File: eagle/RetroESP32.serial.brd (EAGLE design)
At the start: 71.2 x 115 mm, 68 parts, among them J1 AUDIO_JACK_3.5MM_KIT, J2 SPKR, J3 Batt Conn, J5 503182-1852_503182-1852, J6 USB4110-GF-A, Q3 DMG3415U-7, Q4 mmbt2222, Q5 mmbt2222, U1 ESP32-WROVER_ESP32-WROVER, U3 AP2112-3.3, U4 MCP73831T-2ACI/OT, U6 LM4875

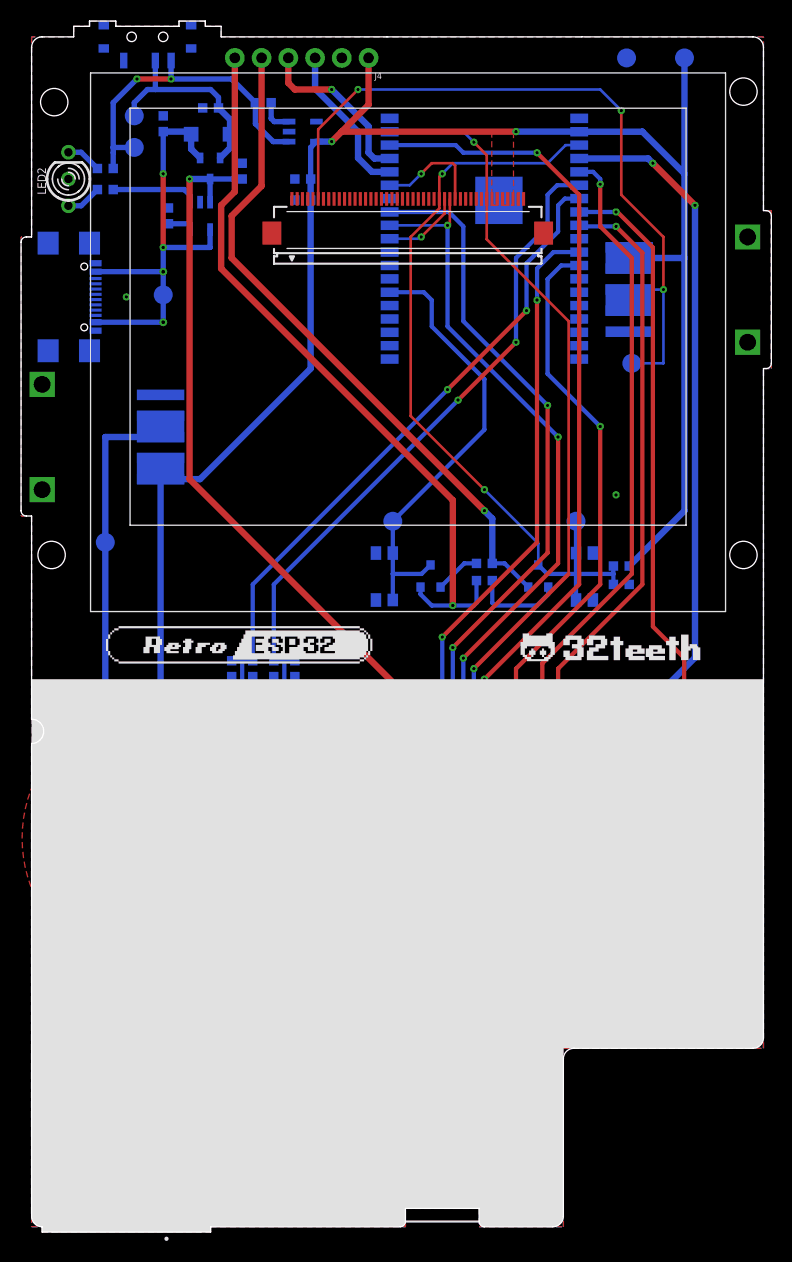
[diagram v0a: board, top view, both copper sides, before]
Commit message: updated CC1/2 pins
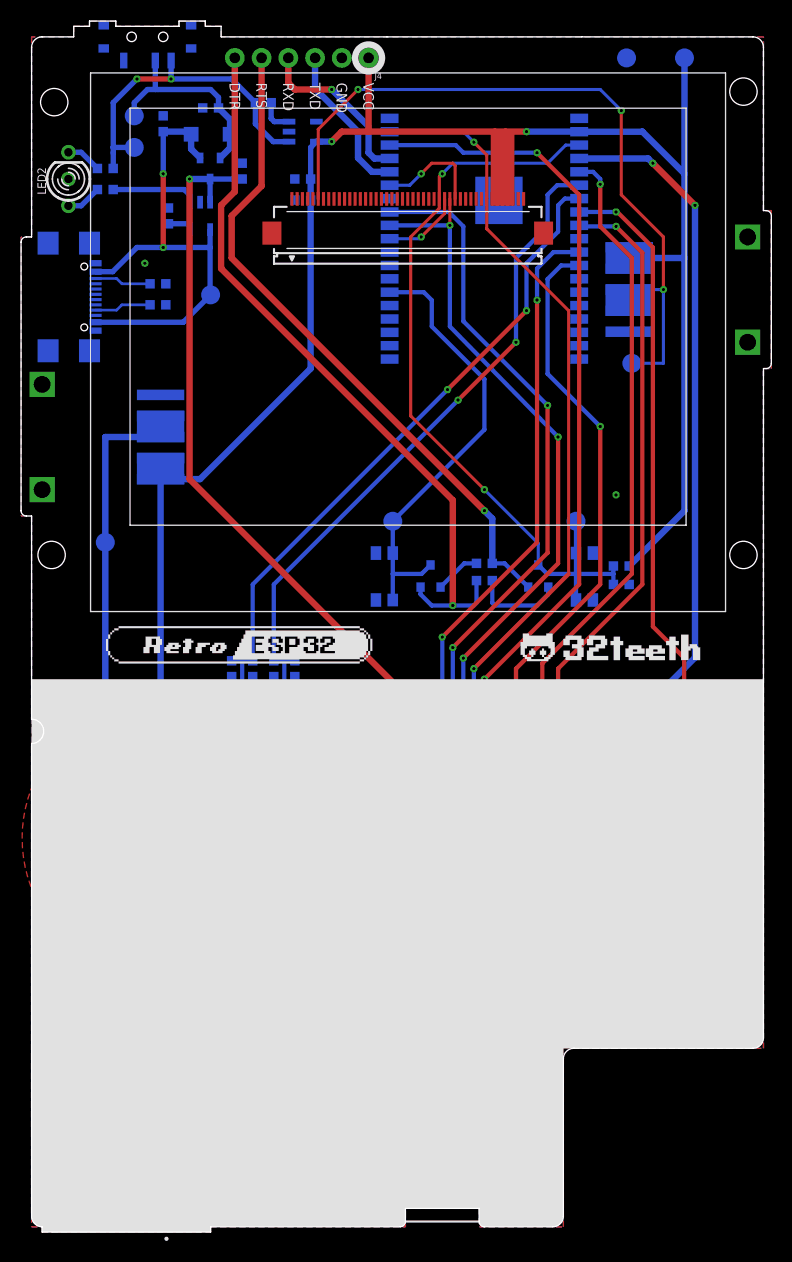
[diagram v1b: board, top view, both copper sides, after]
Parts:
- added R22, R24: 5.1K, RetroESP32:0603-MINI
- R1: value 4.7K -> 1.5K
- U3: value AP2112-3.3 -> XC6210B332MR-G
- U4: value MCP73831T-2ACI/OT -> MCP73832T-2ACI/OT
- moved VBUS 4.50 mm to (17.0, 88.5)
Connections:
- new net CC1: J6.A5, R22.2
- new net CC2: J6.B5, R24.2
- net GND: now also J6.A7, J6.B7, R22.1, R24.1
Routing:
- net 3V3: track 267.3 -> 299.7 mm
- net CC2: track 0.00 -> 5.38 mm
- net CC1: track 0.00 -> 5.38 mm
- net VBUS: track 42.5 -> 46.4 mm, vias 4 -> 2
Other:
- board text added: "DTR"
- board text added: "RTS"
- board text added: "RXD"
- board text added: "TXD"
- board text added: "VCC"
